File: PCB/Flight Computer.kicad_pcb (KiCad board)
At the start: 6 copper layers, 30 x 60 mm, 88 parts, among them J501 Conn_02x03_Counter_Clockwise, J502 USB_C_Receptacle_USB2.0_16P, J503 Screw_Terminal_01x06, J504 Screw_Terminal_01x04, J505 Conn_01x04, J506 Conn_02x03_Counter_Clockwise, J507 Conn_01x06, J601 Conn_Coaxial, Q1 SL2302S, Q701 SL2302S, Q702 SL2302S, Q703 SL2302S, U201 LM1117MP-3.3, U301 W25Q128JVS, U302 STM32F446RETx, U401 MMC5633NJL, U402 LSM6DSV320, U403 MS5607-02BA, U404 SAM-M8Q, U601 RFM95W-915S2, Y301 Resonator

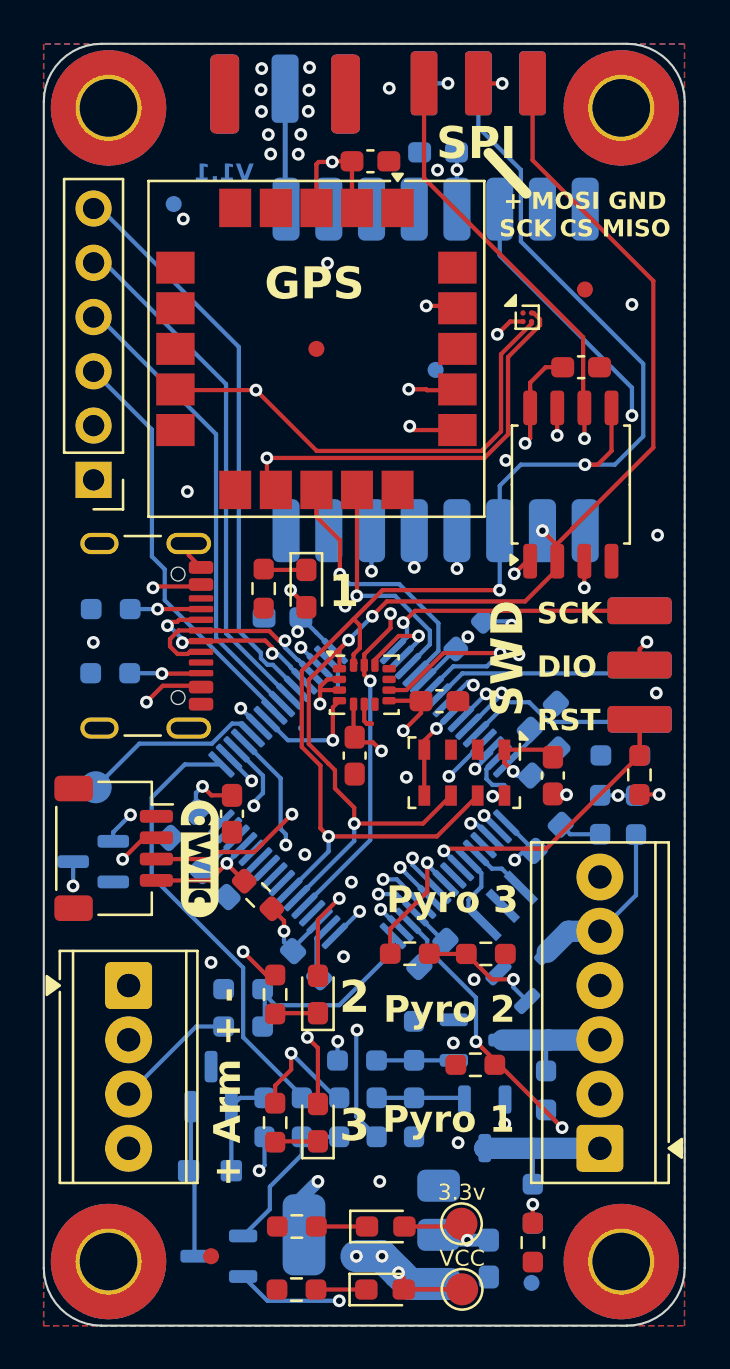
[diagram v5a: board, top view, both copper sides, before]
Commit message: Moved magnetometer slightly, updated routing more
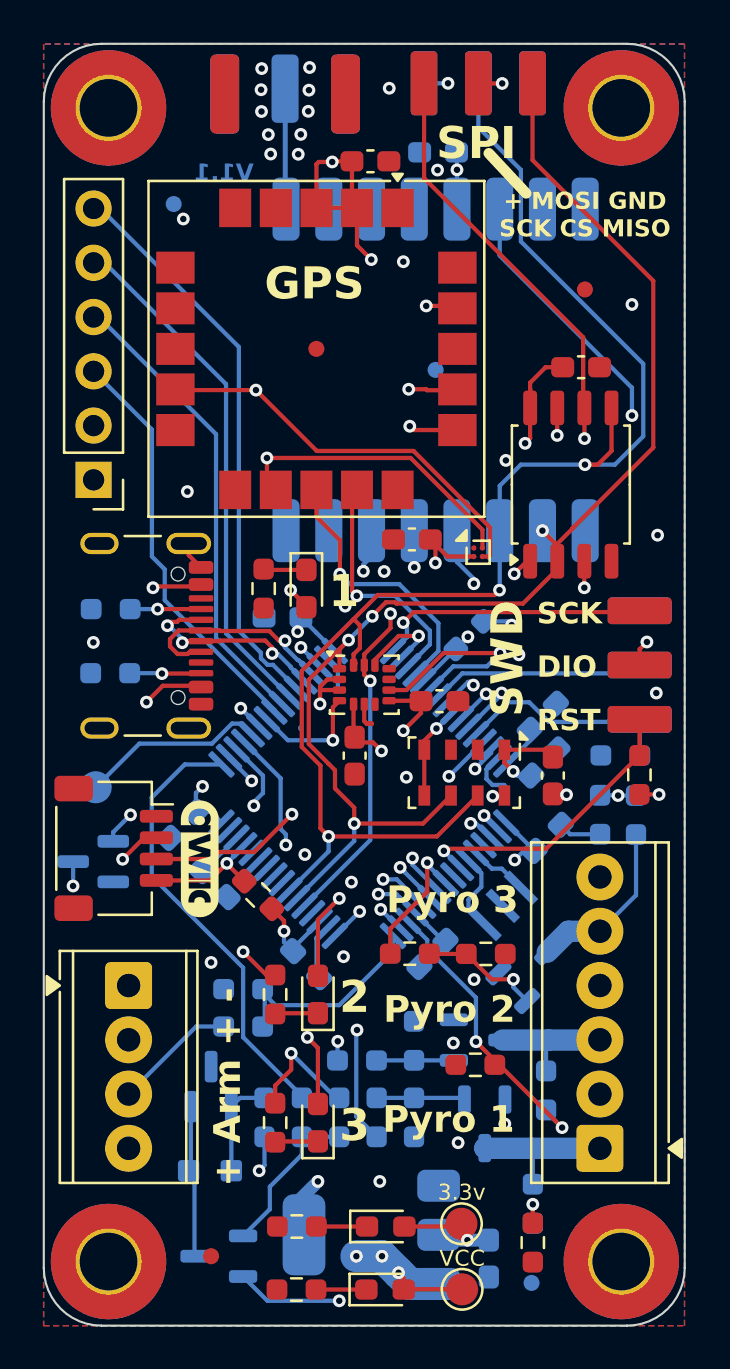
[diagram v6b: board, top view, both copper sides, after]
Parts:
- moved C403 15.4 mm to (114.9, 75.7), turned to 180 degrees
- moved U401 11.2 mm to (118.0, 76.3)
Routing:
- net /I2C_SCL: track 48.5 -> 42.6 mm
- net +3.3V: track 66.1 -> 71.1 mm, vias 20 -> 21
- net /I2C_SDA: track 60.1 -> 56.6 mm
- net /SPI_SCK: track 58.2 -> 60.1 mm
- net GND: vias 39 -> 40

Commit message: Added more GND vias around mosfets for pyro channels
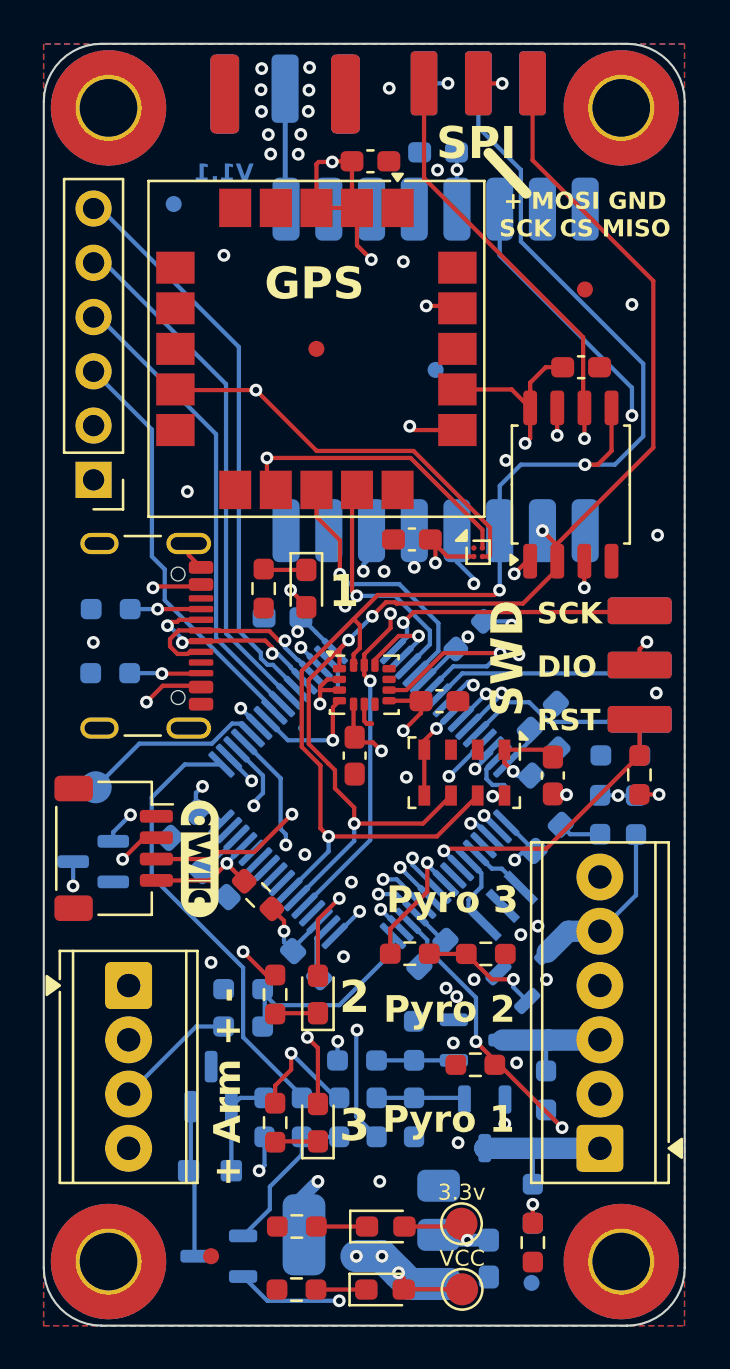
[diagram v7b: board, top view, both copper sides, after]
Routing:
- net +3.3V: track 71.1 -> 72.5 mm, vias 21 -> 20
- net GND: vias 40 -> 46
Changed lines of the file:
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@@
+	)
+	(via
+		(at 119.8 100.2)
+		(size 0.6)
+		(drill 0.3)
+		(layers "F.Cu" "B.Cu")
+		(free yes)
+		(net 1)
 	)
 	(via
@@
 	)
 	(via
+		(at 120.8 93.8)
+		(size 0.6)
+		(drill 0.3)
+		(layers "F.Cu" "B.Cu")
+		(free yes)
+		(net 1)
+	)
+	(via
 		(at 108.18 56.75)
 		(size 0.6)
@@
 	)
 	(via
+		(at 116.5 96.7)
+		(size 0.6)
+		(drill 0.3)
+		(layers "F.Cu" "B.Cu")
+		(free yes)
+		(net 1)
+	)
+	(via
 		(at 113.84 54.58)
 		(size 0.6)
@@
 	)
 	(via
+		(at 117 97.1)
+		(size 0.6)
+		(drill 0.3)
+		(layers "F.Cu" "B.Cu")
+		(free yes)
+		(net 1)
+	)
+	(via
 		(at 109.7 56.74)
 		(size 0.6)
@@
 	)
 	(via
-		(at 104.2 60.7)
+		(at 121.2 96.3)
+		(size 0.6)
+		(drill 0.3)
+		(layers "F.Cu" "B.Cu")
+		(free yes)
+		(net 1)
+	)
+	(via
+		(at 120 94.2)
+		(size 0.6)
+		(drill 0.3)
+		(layers "F.Cu" "B.Cu")
+		(free yes)
+		(net 1)
+	)
+	(via
+		(at 106.1 62.4)
 		(size 0.6)
 		(drill 0.3)
@@
 	)
 	(segment
+		(start 117.03 68.68)
+		(end 119.5725 68.68)
+		(width 0.2)
+		(layer "F.Cu")
+		(net 2)
+	)
+	(segment
 		(start 117.8 76.5)
 		(end 116.562501 76.5)
@@
 	)
 	(segment
-		(start 116.439918 68.68)
-		(end 117.03 68.68)
-		(width 0.2)
-		(layer "F.Cu")
-		(net 2)
-	)
-	(segment
 		(start 119.641714 86.558286)
 		(end 119.23 86.146572)
@@
 	)
 	(segment
-		(start 115.570082 68.67)
-		(end 115.616082 68.716)
-		(width 0.2)
-		(layer "F.Cu")
-		(net 2)
-	)
-	(segment
 		(start 120.435 69.5425)
 		(end 120.435 70.965)
@@
 	)
 	(segment
+		(start 119.5725 68.68)
+		(end 120.435 69.5425)
+		(width 0.2)
+		(layer "F.Cu")
+		(net 2)
+	)
+	(segment
 		(start 117.27 108.5)
 		(end 116.63 107.86)
@@
 	)
 	(segment
-		(start 114.75 68.67)
-		(end 115.570082 68.67)
-		(width 0.2)
-		(layer "F.Cu")
-		(net 2)
-	)
-	(segment
-		(start 116.403918 68.716)
-		(end 116.439918 68.68)
-		(width 0.2)
-		(layer "F.Cu")
-		(net 2)
-	)
-	(segment
 		(start 112.095 59.945)
 		(end 112.33 60.18)
@@
 		(net 2)
 	)
-	(segment
-		(start 115.616082 68.716)
-		(end 116.403918 68.716)
-		(width 0.2)
-		(layer "F.Cu")
-		(net 2)
-	)
 	(via
 		(at 108.915 94.035)
@@
 		(size 0.6)
 		(drill 0.3)
-		(layers "F.Cu" "B.Cu")
-		(net 2)
-	)
-	(via
-		(at 114.75 68.67)
-		(size 0.6)
-		(drill 0.3)

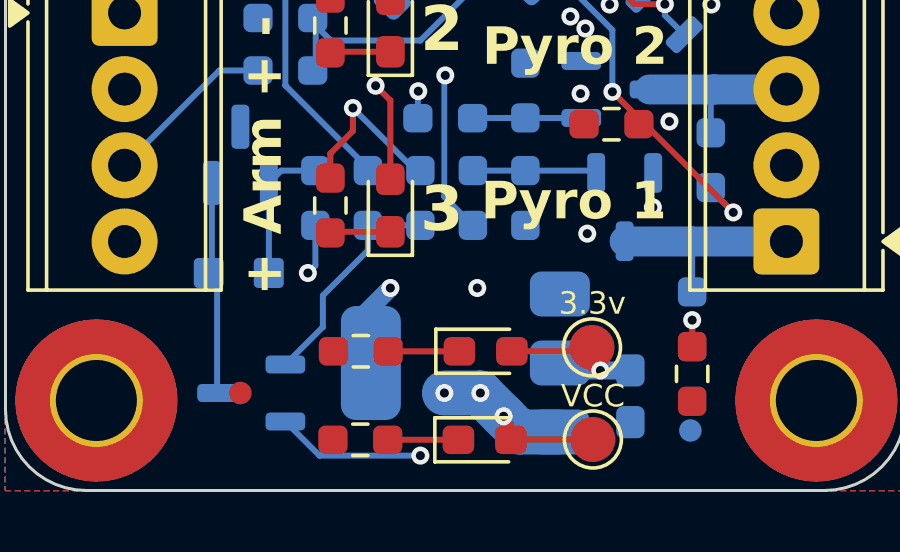
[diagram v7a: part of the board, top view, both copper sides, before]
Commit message: Finalized buzzer footprint and minor tweaks
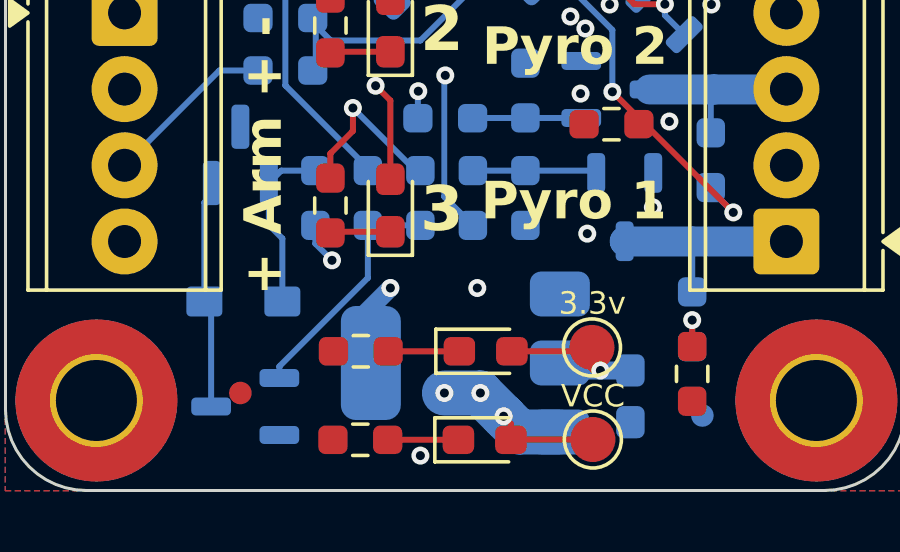
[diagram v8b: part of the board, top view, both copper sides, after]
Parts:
- moved BZ501 0.96 mm to (105.6, 106.2)
- moved FID203 0.64 mm to (120.9, 110.0)
- moved Q1 0.49 mm to (105.7, 109.7)
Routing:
- net GND: track 31.7 -> 26.7 mm
- net Net-(BZ501-+): track 4.73 -> 5.86 mm
- net Net-(Q1-G): track 7.53 -> 8.06 mm
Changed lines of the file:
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@@
 	(footprint "Buzzer:Buzzer_3mm"
 		(layer "B.Cu")
-		(at 105.44738 105.25 180)
+		(at 105.6 106.2 180)
 		(descr "https://www.cui.com/product/resource/cpt-9019s-smt.pdf")
 		(tags "buzzer piezo")
@@
 		(attr smd)
 		(fp_line
-			(start 1.7 1.7)
-			(end -1.1 1.7)
+			(start 2 1.1)
+			(end 2 -1.7)
 			(stroke
 				(width 0.1)
@@
 		)
 		(fp_line
-			(start 1.7 -1.7)
-			(end 1.7 1.7)
+			(start 2 -1.7)
+			(end -2 -1.7)
 			(stroke
 				(width 0.1)
@@
 		)
 		(fp_line
-			(start -1.1 1.7)
-			(end -1.7 1.1)
+			(start 1.4 1.7)
+			(end 2 1.1)
 			(stroke
 				(width 0.1)
@@
 		)
 		(fp_line
-			(start -1.7 1.1)
-			(end -1.7 -1.7)
+			(start -2 1.7)
+			(end 1.4 1.7)
 			(stroke
 				(width 0.1)
@@
 		)
 		(fp_line
-			(start -1.7 -1.7)
-			(end 1.7 -1.7)
+			(start -2 -1.7)
+			(end -2 1.7)
 			(stroke
 				(width 0.1)
@@
 		)
 		(fp_line
-			(start 1.7 1.7)
-			(end 1.7 -1.7)
+			(start 2 1.1)
+			(end 1.4 1.7)
 			(stroke
 				(width 0.1)
@@
 		)
 		(fp_line
-			(start 1.7 -1.7)
-			(end -1.7 -1.7)
+			(start 2 -1.7)
+			(end 2 1.1)
 			(stroke
 				(width 0.1)
@@
 		)
 		(fp_line
-			(start -1.1 1.7)
-			(end 1.7 1.7)
+			(start 1.4 1.7)
+			(end -2 1.7)
 			(stroke
 				(width 0.1)
@@
 		)
 		(fp_line
-			(start -1.7 1.1)
-			(end -1.1 1.7)
+			(start -2 1.7)
+			(end -2 -1.7)
 			(stroke
 				(width 0.1)
@@
 		)
 		(fp_line
-			(start -1.7 -1.7)
-			(end -1.7 1.1)
+			(start -2 -1.7)
+			(end 1.9 -1.7)
 			(stroke
 				(width 0.1)
@@
 		)
 		(fp_line
-			(start 1.8 1.8)
-			(end 1.8 -1.8)
+			(start 2.1 1.2)
+			(end 1.5 1.8)
 			(stroke
 				(width 0.05)
@@
 		)
 		(fp_line
-			(start 1.8 -1.8)
-			(end -1.8 -1.8)
+			(start 2.1 -1.8)
+			(end 2.1 1.2)
 			(stroke
 				(width 0.05)
@@
 		)
 		(fp_line
-			(start -1.2 1.8)
-			(end 1.8 1.8)
+			(start 1.5 1.8)
+			(end -2.1 1.8)
 			(stroke
 				(width 0.05)
@@
 		)
 		(fp_line
-			(start -1.8 1.2)
-			(end -1.2 1.8)
+			(start -2.1 1.8)
+			(end -2.1 -1.8)
 			(stroke
 				(width 0.05)
@@
 		)
 		(fp_line
-			(start -1.8 -1.8)
-			(end -1.8 1.2)
+			(start -2.1 -1.8)
+			(end 2.1 -1.8)
 			(stroke
 				(width 0.05)
@@
 		)
 		(pad "1" smd roundrect
-			(at -1 0 180)
-			(size 1 1)
+			(at -1.3 0 180)
+			(size 1.2 1)
 			(layers "B.Cu" "B.Mask" "B.Paste")
 			(roundrect_rratio 0.15)
@@
 		)
 		(pad "2" smd roundrect
-			(at 1 0 180)
-			(size 1 1)
+			(at 1.3 0 180)
+			(size 1.2 1)
 			(layers "B.Cu" "B.Mask" "B.Paste")
 			(roundrect_rratio 0.15)
@@
 	(footprint "Package_TO_SOT_SMD:SOT-23-3"
 		(layer "B.Cu")
-		(at 105.8625 109.25 180)
+		(at 105.6625 109.7 180)
 		(descr "SOT, 3 Pin (JEDEC MO-178 inferred 3-pin variant https://www.jedec.org/document_search?search_api_views_fulltext=MO-178), generated with kicad-footprint-generator ipc_gullwing_generator.py")
 		(tags "SOT TO_SOT_SMD")
@@
 	(footprint "Fiducial:Fiducial_0.75mm_Mask1.5mm"
 		(layer "B.Cu")
-		(at 120.5 110.5 180)
+		(at 120.9 110 180)
 		(descr "Fiducial, circular marking, 0.75mm bare copper, 1.5mm soldermask opening (Level B)")
 		(tags "fiducial")
@@
 	)
 	(segment
-		(start 107 110.2)
-		(end 108.137 111.337)
-		(width 0.2)
-		(layer "B.Cu")
-		(net 1)
-	)
-	(segment
 		(start 114.193374 91.610482)
 		(end 115.426446 92.843554)
@@
 	)
 	(segment
-		(start 108.137 111.337)
-		(end 111.5 111.337)
-		(width 0.2)
-		(layer "B.Cu")
-		(net 1)
-	)
-	(segment
 		(start 111.5 101.8375)
 		(end 111.3375 101.8375)
@@
 	)
 	(via
-		(at 107.75 105.25)
+		(at 108.553818 104.827)
 		(size 0.6)
 		(drill 0.3)
@@
 	)
 	(segment
-		(start 108 105)
-		(end 107.75 105.25)
+		(start 108 104.273182)
+		(end 108 103.6625)
 		(width 0.2)
 		(layer "B.Cu")
@@
 	)
 	(segment
+		(start 108.553818 104.827)
+		(end 108 104.273182)
+		(width 0.2)
+		(layer "B.Cu")
+		(net 2)
+	)
+	(segment
 		(start 108.915 94.035)
 		(end 108.915 94.545)
@@
 	)
 	(segment
-		(start 108 103.6625)
-		(end 108 105)
-		(width 0.2)
-		(layer "B.Cu")
-		(net 2)
-	)
-	(segment
 		(start 120.49012 86.74988)
 		(end 119.833308 86.74988)
@@
 	)
 	(segment
-		(start 104.725 105.52762)
-		(end 104.44738 105.25)
+		(start 104.525 106.425)
+		(end 104.3 106.2)
 		(width 0.2)
 		(layer "B.Cu")
@@
 	)
 	(segment
-		(start 104.3625 105.58488)
-		(end 104.44738 105.5)
+		(start 104.55 102.65)
+		(end 104.3 102.9)
 		(width 0.2)
 		(layer "B.Cu")
@@
 	)
 	(segment
-		(start 104.55 102.25)
-		(end 104.55 105.14738)
+		(start 104.3 102.9)
+		(end 104.3 106.2)
 		(width 0.2)
 		(layer "B.Cu")
@@
 	)
 	(segment
-		(start 104.725 109.25)
-		(end 104.725 105.52762)
+		(start 104.525 109.7)
+		(end 104.525 106.425)
 		(width 0.2)
 		(layer "B.Cu")
@@
 	)
 	(segment
-		(start 104.55 105.14738)
-		(end 104.44738 105.25)
+		(start 104.55 102.25)
+		(end 104.55 102.65)
 		(width 0.2)
 		(layer "B.Cu")
@@
 	)
 	(segment
-		(start 106.44738 104.80262)
-		(end 106.45 104.8)
-		(width 0.2)
-		(layer "B.Cu")
-		(net 84)
-	)
-	(segment
-		(start 106.44738 105.25)
-		(end 106.44738 104.80262)
+		(start 106.8625 101.8375)
+		(end 108 101.8375)
 		(width 0.2)
 		(layer "B.Cu")
@@
 	)
 	(segment
-		(start 106.45 105.24738)
-		(end 106.44738 105.25)
+		(start 106.9 106.2)
+		(end 106.9 104.1)
 		(width 0.2)
 		(layer "B.Cu")
@@
 	)
 	(segment
-		(start 106.45 104.8)
-		(end 106.45 102.25)
+		(start 106.45 102.25)
+		(end 106.45 103.65)
 		(width 0.2)
 		(layer "B.Cu")
@@
 	)
 	(segment
-		(start 106.8625 101.8375)
-		(end 108 101.8375)
+		(start 106.45 103.65)
+		(end 106.9 104.1)
 		(width 0.2)
 		(layer "B.Cu")
@@
 	)
 	(segment
-		(start 109.75 103.6625)
-		(end 111.5 103.6625)
+		(start 106.8 108.75)
+		(end 106.8 108.363181)
 		(width 0.2)
 		(layer "B.Cu")
@@
 	(segment
 		(start 109.75 103.6625)
-		(end 109.75 104.5)
-		(width 0.2)
-		(layer "B.Cu")
-		(net 87)
-	)
-	(segment
-		(start 109.75 104.5)
-		(end 108.25 106)
+		(end 111.5 103.6625)
 		(width 0.2)
 		(layer "B.Cu")
@@
 	)
 	(segment
-		(start 108.25 106)
-		(end 108.25 107.05)
+		(start 109.75 105.413181)
+		(end 106.8 108.363181)
 		(width 0.2)
 		(layer "B.Cu")
@@
 	)
 	(segment
-		(start 108.25 107.05)
-		(end 107 108.3)
+		(start 109.75 103.6625)
+		(end 109.75 105.413181)
 		(width 0.2)
 		(layer "B.Cu")
